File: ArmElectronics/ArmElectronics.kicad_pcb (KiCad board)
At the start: 4 copper layers, 101 x 139 mm, 66 parts, among them J1 Raspberry_Pi_2_3, J2 12V In, J3 RasPi Power Out, J4 Batt In, J5 Batt Out, J6 BNO055 QWIIC Conn, J7 Conn_01x14, J8 Conn_01x14, J9 1792245, U1 Teensy4.1, U10 PA-09, U11 74LVC1G97, U12 74LVC1G97, U13 74LVC1G97, U14 74LVC1G97, U15 74LVC1G97, U16 74LVC1G97, U2 Pololu_2857, U3 Pololu_2851, U4 Pololu_3730, U5 TB9051FTG, U6 TB9051FTG, U7 TB9051FTG, U8 PA-09, U9 PA-09

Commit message: I think it worked?
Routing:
- net +3V3: track 61.0 -> 245.5 mm, vias 15 -> 13
- net +5V: track 333.6 -> 295.3 mm, vias 0 -> 3
- net (no net): track 27.0 -> 0.00 mm, vias 4 -> 0
- net GND: track 0.00 -> 12.3 mm, vias 19 -> 51
- net /Teensy_SCL2: track 51.3 -> 55.1 mm
- net /Teensy_SDA2: track 52.3 -> 54.7 mm
- removed copper zone on In2.Cu, net +3V3
- removed copper zone on In1.Cu, net GND
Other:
- copper layers 4 -> 2

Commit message: Tweaks
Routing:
- net GND: vias 51 -> 55
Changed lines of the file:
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@@
     (thickness 1.6)
     (drawings 4)
-    (tracks 735)
+    (tracks 739)
     (zones 0)
     (modules 66)
@@
   (via (at 192.8 109.6) (size 0.6) (drill 0.3) (layers F.Cu B.Cu) (net 5))
   (via (at 247.4 108.2) (size 1) (drill 0.5) (layers F.Cu B.Cu) (net 5))
-  (via (at 250 108.2) (size 1) (drill 0.5) (layers F.Cu B.Cu) (net 5))
+  (via (at 250.2 108.2) (size 1) (drill 0.5) (layers F.Cu B.Cu) (net 5))
   (via (at 247.4 111) (size 1) (drill 0.5) (layers F.Cu B.Cu) (net 5))
-  (via (at 250 111) (size 1) (drill 0.5) (layers F.Cu B.Cu) (net 5))
+  (via (at 250.2 111) (size 1) (drill 0.5) (layers F.Cu B.Cu) (net 5))
   (via (at 223.8 97.6) (size 1) (drill 0.5) (layers F.Cu B.Cu) (net 5))
   (via (at 220.4 97.6) (size 1) (drill 0.5) (layers F.Cu B.Cu) (net 5))
@@
   (via (at 204 27.8) (size 1) (drill 0.5) (layers F.Cu B.Cu) (net 5))
   (via (at 270 103.8) (size 1) (drill 0.5) (layers F.Cu B.Cu) (net 5))
-  (via (at 272 103.8) (size 1) (drill 0.5) (layers F.Cu B.Cu) (net 5))
+  (via (at 271.4 103.8) (size 1) (drill 0.5) (layers F.Cu B.Cu) (net 5))
   (via (at 270 107.8) (size 1) (drill 0.5) (layers F.Cu B.Cu) (net 5))
-  (via (at 272 107.8) (size 1) (drill 0.5) (layers F.Cu B.Cu) (net 5))
+  (via (at 271.4 107.8) (size 1) (drill 0.5) (layers F.Cu B.Cu) (net 5))
+  (via (at 248.8 108.2) (size 1) (drill 0.5) (layers F.Cu B.Cu) (net 5))
+  (via (at 248.8 111) (size 1) (drill 0.5) (layers F.Cu B.Cu) (net 5))
+  (via (at 272.8 103.8) (size 1) (drill 0.5) (layers F.Cu B.Cu) (net 5))
+  (via (at 272.8 107.8) (size 1) (drill 0.5) (layers F.Cu B.Cu) (net 5))
   (segment (start 189.87 71.87) (end 191.14 70.6) (width 0.2) (layer B.Cu) (net 8))
   (segment (start 186.400033 73.599967) (end 188.13 71.87) (width 0.2) (layer B.Cu) (net 8))

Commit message: Added text
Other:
- board text added: "12V In"
- board text added: "2020-2022"
- board text added: "Actuator 1"
- board text added: "Actuator 2"
- board text added: "Actuator 3"
- board text added: "Arm Base PCB r1 UAH SHC ASTRA"
- board text added: "Battery In"
- board text added: "Battery Out"
- board text added: "QWIIC (IMU)"
- board text added: "RPi Expansion Header"
- board text added: "Stepper"
- board text added: "Teensy Expansion Header"
- board text added: "USB Power Out"

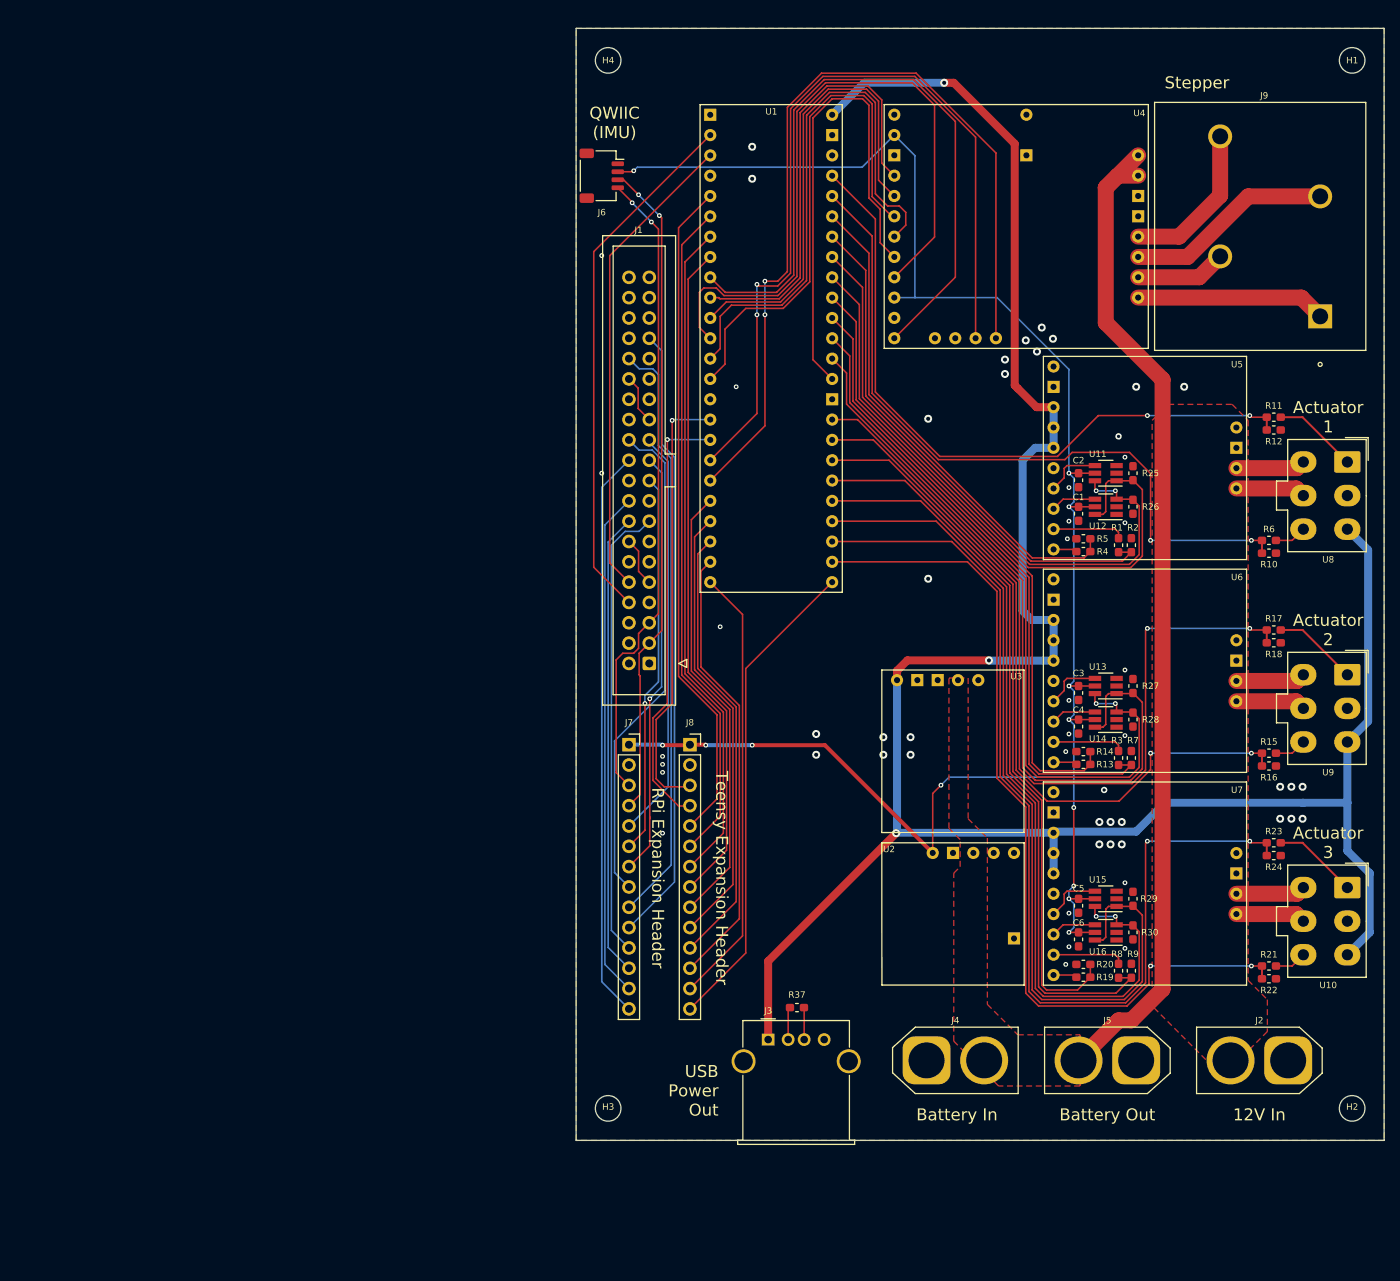
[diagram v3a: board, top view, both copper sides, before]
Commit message: Updated PCB for new schematic
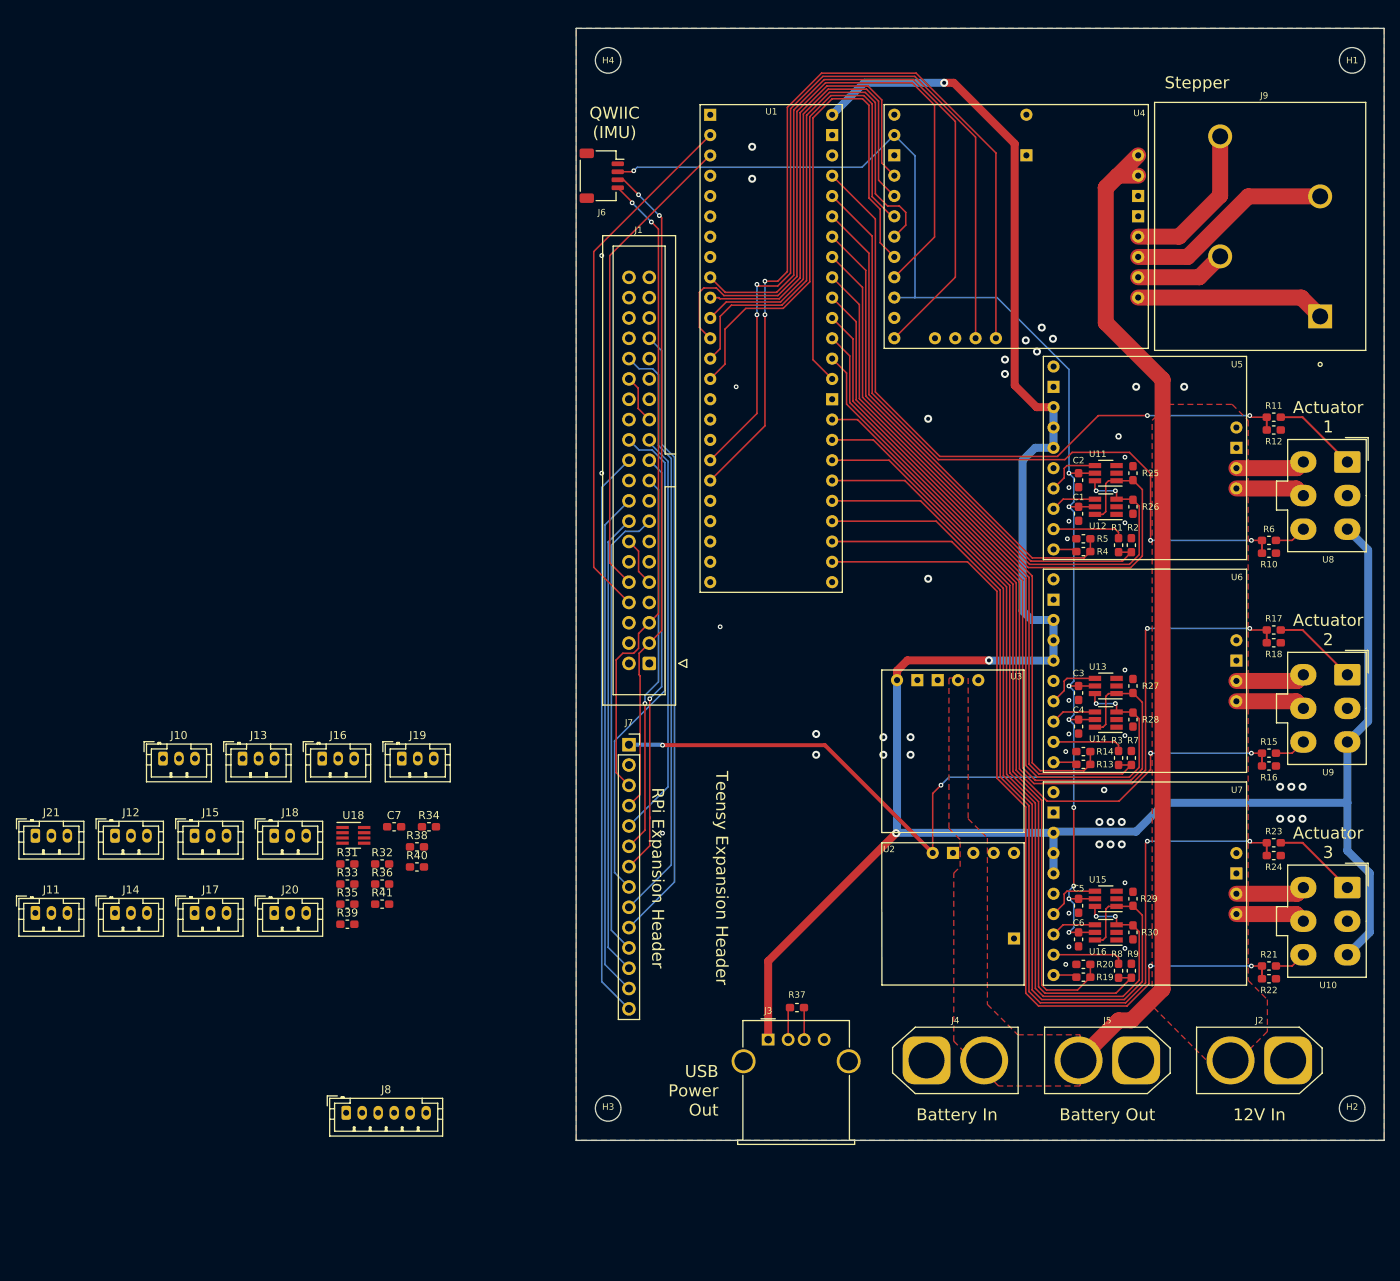
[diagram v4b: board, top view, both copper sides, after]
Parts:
- added C7: 0.1u, Capacitor_SMD:C_0603_1608Metric_Pad1.05x0.95mm_HandSolder, F.Cu at (159.2, 108.8)
- added J10: AH1815 Breakout, Connector_JST:JST_PH_B3B-PH-K_1x03_P2.00mm_Vertical, F.Cu at (130.3, 100.3)
- added J11: AH1815 Breakout, Connector_JST:JST_PH_B3B-PH-K_1x03_P2.00mm_Vertical, F.Cu at (114.4, 119.6)
- added J12: AH1815 Breakout, Connector_JST:JST_PH_B3B-PH-K_1x03_P2.00mm_Vertical, F.Cu at (124.3, 109.9)
- added J13: AH1815 Breakout, Connector_JST:JST_PH_B3B-PH-K_1x03_P2.00mm_Vertical, F.Cu at (140.3, 100.3)
- added J14: AH1815 Breakout, Connector_JST:JST_PH_B3B-PH-K_1x03_P2.00mm_Vertical, F.Cu at (124.3, 119.6)
- added J15: AH1815 Breakout, Connector_JST:JST_PH_B3B-PH-K_1x03_P2.00mm_Vertical, F.Cu at (134.3, 109.9)
- added J16: AH1815 Breakout, Connector_JST:JST_PH_B3B-PH-K_1x03_P2.00mm_Vertical, F.Cu at (150.2, 100.3)
- added J17: AH1815 Breakout, Connector_JST:JST_PH_B3B-PH-K_1x03_P2.00mm_Vertical, F.Cu at (134.3, 119.6)
- added J18: AH1815 Breakout, Connector_JST:JST_PH_B3B-PH-K_1x03_P2.00mm_Vertical, F.Cu at (144.2, 109.9)
- added J19: AH1815 Breakout, Connector_JST:JST_PH_B3B-PH-K_1x03_P2.00mm_Vertical, F.Cu at (160.2, 100.3)
- added J20: AH1815 Breakout, Connector_JST:JST_PH_B3B-PH-K_1x03_P2.00mm_Vertical, F.Cu at (144.2, 119.6)
- added J21: AH1815 Breakout, Connector_JST:JST_PH_B3B-PH-K_1x03_P2.00mm_Vertical, F.Cu at (114.4, 109.9)
- added R31: 230k, Resistor_SMD:R_0603_1608Metric_Pad1.05x0.95mm_HandSolder, F.Cu at (153.4, 113.5)
- added R32: 62k, Resistor_SMD:R_0603_1608Metric_Pad1.05x0.95mm_HandSolder, F.Cu at (157.8, 113.5)
- added R33: 20k, Resistor_SMD:R_0603_1608Metric_Pad1.05x0.95mm_HandSolder, F.Cu at (153.4, 116.0)
- added R34: 20k, Resistor_SMD:R_0603_1608Metric_Pad1.05x0.95mm_HandSolder, F.Cu at (163.6, 108.8)
- added R35: 10k, Resistor_SMD:R_0603_1608Metric_Pad1.05x0.95mm_HandSolder, F.Cu at (153.4, 118.5)
- added R36: 10k, Resistor_SMD:R_0603_1608Metric_Pad1.05x0.95mm_HandSolder, F.Cu at (157.8, 116.0)
- added R38: 10k, Resistor_SMD:R_0603_1608Metric_Pad1.05x0.95mm_HandSolder, F.Cu at (162.1, 111.3)
- added R39: 10k, Resistor_SMD:R_0603_1608Metric_Pad1.05x0.95mm_HandSolder, F.Cu at (153.4, 121.0)
- added R40: 100k, Resistor_SMD:R_0603_1608Metric_Pad1.05x0.95mm_HandSolder, F.Cu at (162.1, 113.8)
- added R41: 100k, Resistor_SMD:R_0603_1608Metric_Pad1.05x0.95mm_HandSolder, F.Cu at (157.8, 118.5)
- added U18: MAX11601, Package_TO_SOT_SMD:SOT-23-8_Handsoldering, F.Cu at (154.2, 109.9)
- J8: value Conn_01x14 -> Encoder Breakout; footprint Connector_PinSocket_2.54mm:PinSocket_1x14_P2.54mm_Vertical -> Connector_JST:JST_PH_B6B-PH-K_1x06_P2.00mm_Vertical
- moved J8 63.0 mm to (153.2, 144.6)
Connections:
- J1 pad 1: Net-(J1-Pad1) -> (no net)
- J1 pad 11: Net-(J1-Pad11) -> (no net)
- J1 pad 12: Net-(J1-Pad12) -> (no net)
- J1 pad 13: Net-(J1-Pad13) -> (no net)
- J1 pad 17: Net-(J1-Pad17) -> (no net)
- J1 pad 2: Net-(J1-Pad2) -> (no net)
- J1 pad 26: Net-(J1-Pad26) -> (no net)
- J1 pad 27: Net-(J1-Pad27) -> (no net)
- J1 pad 28: Net-(J1-Pad28) -> (no net)
- J1 pad 29: Net-(J1-Pad29) -> (no net)
- J1 pad 31: Net-(J1-Pad31) -> (no net)
- J1 pad 35: Net-(J1-Pad35) -> (no net)
- J1 pad 36: Net-(J1-Pad36) -> (no net)
- J1 pad 37: Net-(J1-Pad37) -> (no net)
- J1 pad 38: Net-(J1-Pad38) -> (no net)
- J1 pad 4: Net-(J1-Pad4) -> (no net)
- J1 pad 40: Net-(J1-Pad40) -> (no net)
- J1 pad 7: Net-(J1-Pad7) -> (no net)
- J8 pad 3: /Teensy_SCL2 -> /Teensy_MOSI0
- J8 pad 4: /Teensy_SDA2 -> /Teensy_MISO0
- J8 pad 5: /Teensy_GPIO3 -> /Teensy_SCK0
- J8 pad 6: /Teensy_GPIO4 -> /Encoder_CS
- U1 pad 15: Net-(U1-Pad15) -> (no net)
- U1 pad 28: Net-(U1-Pad28) -> (no net)
- U1 pad 31: /Teensy_SCL2 -> /Encoder_CS
- U1 pad 32: /Teensy_SDA2 -> /Hall_SW_6
- U1 pad 35: /Teensy_GPIO28 -> /Hall_SW_7
- U1 pad 36: /Teensy_GPIO29 -> /Hall_SW_8
- U1 pad 37: /Teensy_GPIO30 -> /Hall_SW_9
- U1 pad 38: /Teensy_GPIO31 -> /Hall_SW_10
- U1 pad 39: /Teensy_GPIO32 -> /Hall_SW_11
- U1 pad 4: Net-(U1-Pad4) -> /Hall_SW_1
- U1 pad 40: /Teensy_GPIO33 -> /Hall_SW_12
- U1 pad 5: /Teensy_GPIO3 -> /Hall_SW_2
- U1 pad 6: /Teensy_GPIO4 -> /Hall_SW_3
- U1 pad 7: /Teensy_GPIO5 -> /Hall_SW_4
- U1 pad 8: /Teensy_GPIO6 -> /Hall_SW_5
- U2 pad 1: Net-(U2-Pad1) -> (no net)
- U2 pad 2: Net-(U2-Pad2) -> (no net)
- U3 pad 1: Net-(U3-Pad1) -> (no net)
- U4 pad 1: Net-(U4-Pad1) -> (no net)
- U4 pad 11: Net-(U4-Pad11) -> (no net)
- U4 pad 13: Net-(U4-Pad13) -> (no net)
- U4 pad 14: Net-(U4-Pad14) -> (no net)
- U4 pad 25: Net-(U4-Pad25) -> (no net)
- U4 pad 26: Net-(U4-Pad26) -> (no net)
- U5 pad 1: Net-(U5-Pad1) -> (no net)
- U6 pad 1: Net-(U6-Pad1) -> (no net)
- U7 pad 1: Net-(U7-Pad1) -> (no net)
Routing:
- net /Teensy_GPIO5: track 83.8 -> 0.00 mm
- net /Teensy_GPIO6: track 83.8 -> 0.00 mm
- net /Teensy_GPIO4: track 83.8 -> 0.00 mm
- net /Teensy_GPIO3: track 83.8 -> 0.00 mm
- net /Teensy_GPIO33: track 60.7 -> 0.00 mm
- net /Teensy_GPIO31: track 55.8 -> 0.00 mm
- net /Teensy_GPIO30: track 55.8 -> 0.00 mm
- net /Teensy_GPIO29: track 55.8 -> 0.00 mm
- net /Teensy_GPIO28: track 55.8 -> 0.00 mm
- net /Teensy_GPIO32: track 55.2 -> 0.00 mm
- net /Teensy_SCL2: track 55.1 -> 0.00 mm, vias 1 -> 0
- net /Teensy_SDA2: track 54.7 -> 0.00 mm, vias 1 -> 0
- net +3V3: track 245.5 -> 245.4 mm, vias 13 -> 11
- net GND: vias 55 -> 52

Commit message: reannotated schematic
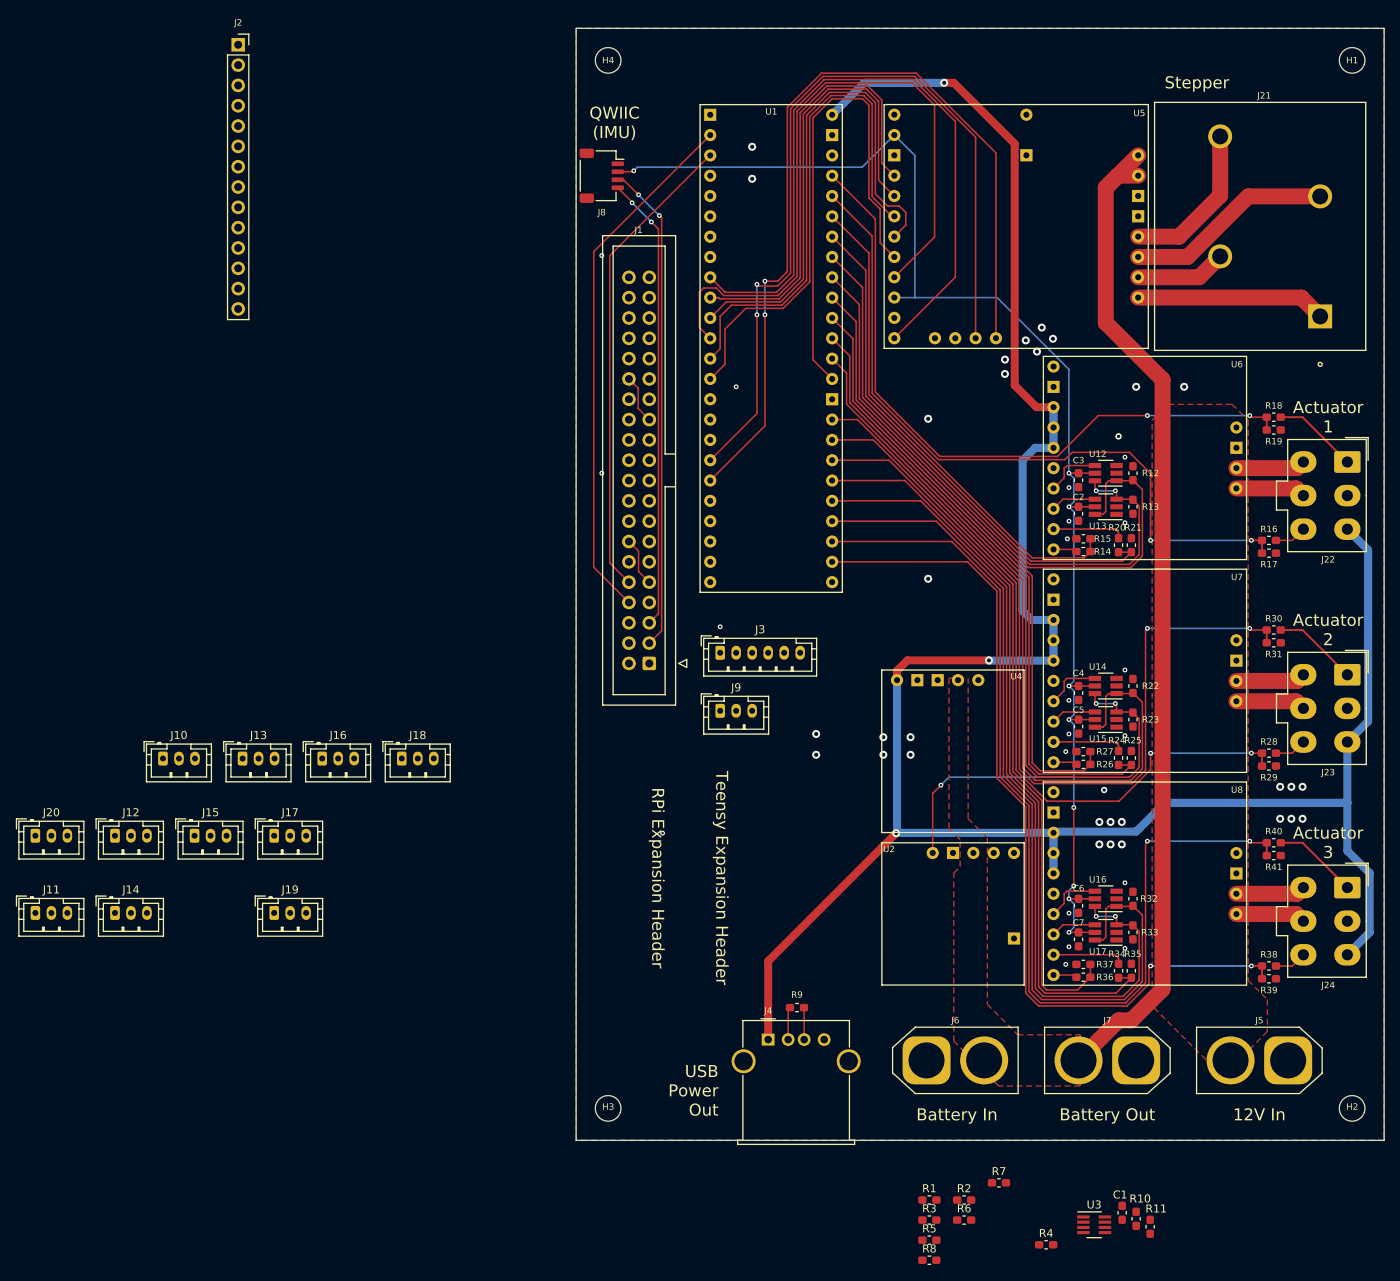
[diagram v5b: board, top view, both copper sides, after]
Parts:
- moved U3 104.6 mm to (246.8, 158.6)
- moved R11 104.1 mm to (253.8, 158.8), turned to 90 degrees
- moved C1 103.0 mm to (250.2, 157.1), turned to 90 degrees
- moved J2 100.2 mm to (139.8, 11.1)
- moved R10 100.1 mm to (252.0, 157.8), turned to 90 degrees
- moved R4 93.2 mm to (240.8, 161.1)
- moved R3 84.0 mm to (226.2, 158.0)
- moved R6 84.0 mm to (230.5, 158.0)
- moved R1 84.0 mm to (226.2, 155.4)
- moved R2 84.0 mm to (230.5, 155.4)
- moved R5 84.0 mm to (226.2, 160.5)
- moved R7 84.0 mm to (234.8, 153.3)
- moved R8 84.0 mm to (226.2, 163.0)
- moved J3 74.1 mm to (200.0, 87.0)
- moved J9 70.4 mm to (200.0, 94.3)
- renumbered C7 to C1, C1 to C2, C2 to C3, C3 to C4, C4 to C5, C5 to C6, C6 to C7, J18 to J17, J19 to J18, J20 to J19, J7 to J2, J21 to J20, J9 to J21, U8 to J22, U9 to J23, U10 to J24, J8 to J3, J3 to J4, J2 to J5, J4 to J6, J5 to J7, J6 to J8, J17 to J9, R31 to R1, R40 to R10, R41 to R11, R25 to R12, R26 to R13, R4 to R14, R5 to R15, R6 to R16, R10 to R17, R11 to R18, R12 to R19, R32 to R2, R1 to R20, R2 to R21, R27 to R22, R28 to R23, R3 to R24, R7 to R25, R13 to R26, R14 to R27, R15 to R28, R16 to R29, R33 to R3, R17 to R30, R18 to R31, R29 to R32, R30 to R33, R8 to R34, R9 to R35, R19 to R36, R20 to R37, R21 to R38, R22 to R39, R34 to R4, R23 to R40, R24 to R41, R35 to R5, R36 to R6, R38 to R7, R39 to R8, R37 to R9, U11 to U12, U12 to U13, U13 to U14, U14 to U15, U15 to U16, U16 to U17, U18 to U3, U3 to U4, U4 to U5, U5 to U6, U6 to U7, U7 to U8
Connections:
- J1 pad 1: (no net) -> Net-(J1-Pad1)
- J1 pad 11: (no net) -> Net-(J1-Pad11)
- J1 pad 12: (no net) -> Net-(J1-Pad12)
- J1 pad 13: (no net) -> Net-(J1-Pad13)
- J1 pad 17: (no net) -> Net-(J1-Pad17)
- J1 pad 2: (no net) -> Net-(J1-Pad2)
- J1 pad 26: (no net) -> Net-(J1-Pad26)
- J1 pad 27: (no net) -> Net-(J1-Pad27)
- J1 pad 28: (no net) -> Net-(J1-Pad28)
- J1 pad 29: (no net) -> Net-(J1-Pad29)
- J1 pad 31: (no net) -> Net-(J1-Pad31)
- J1 pad 35: (no net) -> Net-(J1-Pad35)
- J1 pad 36: (no net) -> Net-(J1-Pad36)
- J1 pad 37: (no net) -> Net-(J1-Pad37)
- J1 pad 38: (no net) -> Net-(J1-Pad38)
- J1 pad 4: (no net) -> Net-(J1-Pad4)
- J1 pad 40: (no net) -> Net-(J1-Pad40)
- J1 pad 7: (no net) -> Net-(J1-Pad7)
- U1 pad 15: (no net) -> Net-(U1-Pad15)
- U1 pad 28: (no net) -> Net-(U1-Pad28)
- U2 pad 1: (no net) -> Net-(U2-Pad1)
- U2 pad 2: (no net) -> Net-(U2-Pad2)
- U4 pad 1: (no net) -> Net-(U4-Pad1)
- U5 pad 1: (no net) -> Net-(U5-Pad1)
- U5 pad 11: (no net) -> Net-(U5-Pad11)
- U5 pad 13: (no net) -> Net-(U5-Pad13)
- U5 pad 14: (no net) -> Net-(U5-Pad14)
- U6 pad 1: (no net) -> Net-(U6-Pad1)
- U7 pad 1: (no net) -> Net-(U7-Pad1)
- U8 pad 1: (no net) -> Net-(U8-Pad1)
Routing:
- net /RPi_GPIO13: track 77.3 -> 0.00 mm
- net /RPi_GPIO12: track 74.0 -> 0.00 mm
- net /RPi_GPIO25: track 71.4 -> 0.00 mm
- net /RPi_GPIO24: track 63.4 -> 0.00 mm
- net /RPi_CS0: track 62.1 -> 0.00 mm
- net /RPi_GPIO23: track 58.0 -> 0.00 mm
- net /RPi_GPI022: track 57.2 -> 0.00 mm
- net /RPi_MISO0: track 53.3 -> 0.00 mm, vias 1 -> 0
- net /RPi_SCLK0: track 51.3 -> 0.00 mm
- net /RPi_MOSI0: track 47.7 -> 0.00 mm, vias 1 -> 0
- net +3V3: track 245.4 -> 201.8 mm, vias 11 -> 10
- net /RPi_SCL: track 80.5 -> 57.0 mm
- net /RPi_SDA: track 82.7 -> 61.3 mm
